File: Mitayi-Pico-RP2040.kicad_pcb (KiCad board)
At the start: 2 copper layers, 21 x 51 mm, 66 parts, among them J1 EXP8, J2 USB_C_Receptacle_USB2.0, J3 Header_1, J4 Header_2, J5 SWD, J6 USB_B_Micro, SW1 Reset, SW2 UBUT, U1 W25Q128JVS, U2 MIC5219-3.3YM5, U3 RP2040, Y1 YIC-12M20P2/XT324-10/10

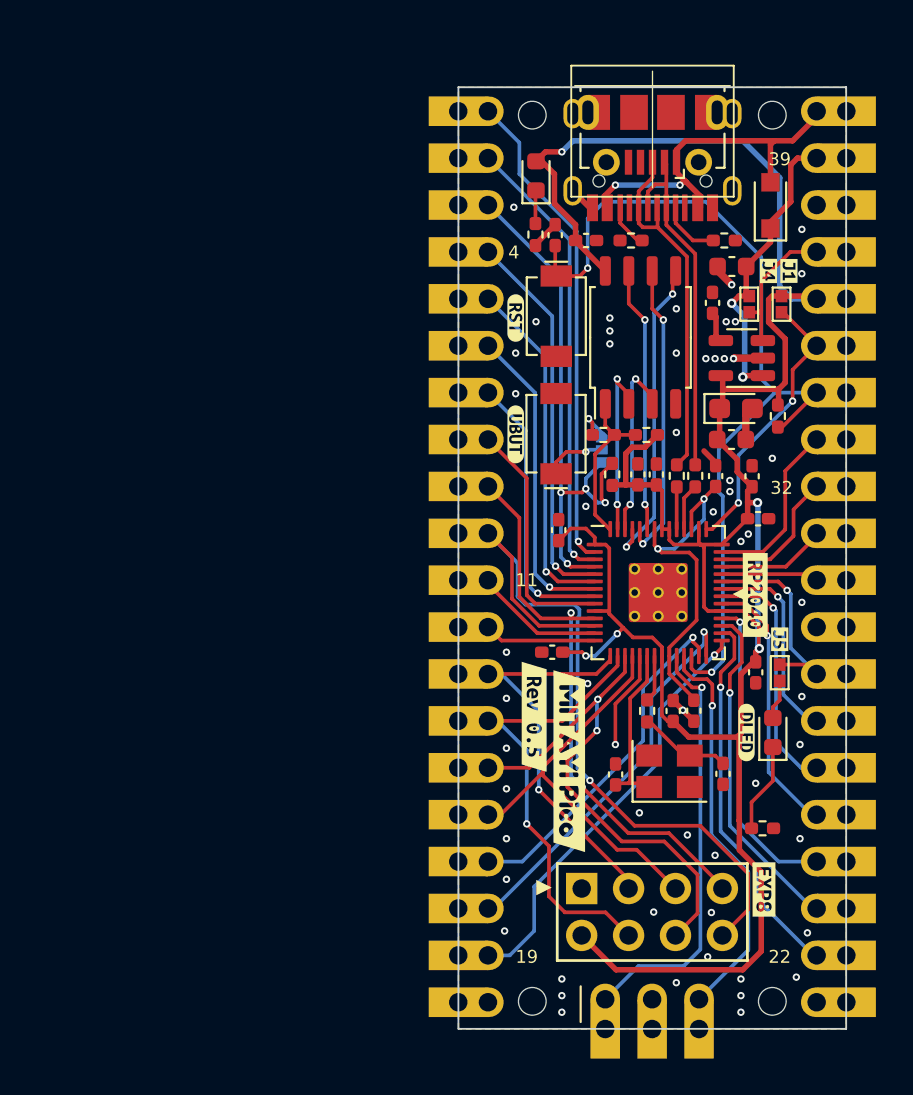
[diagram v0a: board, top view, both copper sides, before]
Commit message: Remove headers and much more
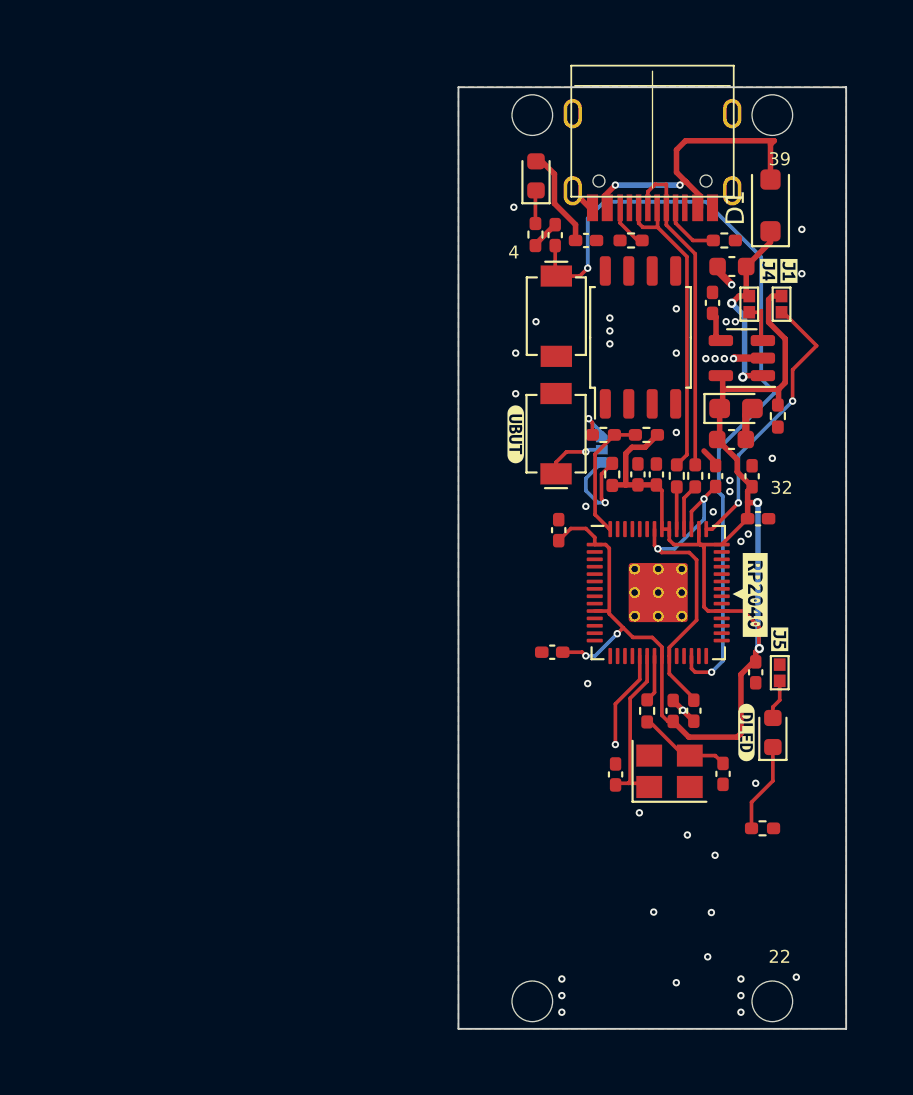
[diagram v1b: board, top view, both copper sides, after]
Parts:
- removed the G*** at (149.1, 89.7)
- removed J1: EXP8, Connector_PinHeader_2.54mm:PinHeader_2x04_P2.54mm_Vertical
- removed J3: Header_1, CIRCUITSTATE-Connector-Pin-Headers:PinHeader_1x20_2H_P2.54mm_Vertical
- removed J4: Header_2, CIRCUITSTATE-Connector-Pin-Headers:PinHeader_1x20_2H_P2.54mm_Vertical
- removed J5: SWD, Connector_PinHeader_2.54mm:PinHeader_1x03_P2.54mm_Vertical
- removed J6: USB_B_Micro, Connector_USB:USB_Micro-B_Molex-105017-0001
- removed kibuzzard-631DCCC7: G***, kibuzzard-631DCCC7
- removed kibuzzard-631DCE29: G***, kibuzzard-631DCE29
- removed kibuzzard-631DD065: G***, kibuzzard-631DD065
- removed kibuzzard-631DD76C: G***, kibuzzard-631DD76C
- removed kibuzzard-632C7F13: G***, kibuzzard-632C7F13
- removed kibuzzard-63B95AA9: G***, kibuzzard-63B95AA9
- D1: footprint Diode_SMD:D_SOD-323_HandSoldering -> Diode_SMD:D_SOD-123F
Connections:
- U1 pad 1: /QSPI_SS -> unconnected-(U1-~{CS}-Pad1)
- U1 pad 2: /QSPI_SD1 -> unconnected-(U1-DO(IO1)-Pad2)
- U1 pad 3: /QSPI_SD2 -> unconnected-(U1-IO2-Pad3)
- U1 pad 4: GND -> unconnected-(U1-GND-Pad4)
- U1 pad 5: /QSPI_SD0 -> unconnected-(U1-DI(IO0)-Pad5)
- U1 pad 6: /QSPI_SCLK -> unconnected-(U1-CLK-Pad6)
- U1 pad 7: /QSPI_SD3 -> unconnected-(U1-IO3-Pad7)
- U1 pad 8: +3V3 -> unconnected-(U1-VCC-Pad8)
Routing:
- net +3V3: track 135.6 -> 84.4 mm, vias 5 -> 4
- net /GPIO9: track 41.1 -> 0.00 mm, vias 1 -> 0
- net /GPIO8: track 31.2 -> 0.00 mm, vias 2 -> 0
- net /GPIO14: track 29.0 -> 0.00 mm, vias 2 -> 0
- net /GPIO0: track 26.5 -> 0.00 mm, vias 1 -> 0
- net /GPIO13: track 25.1 -> 0.00 mm, vias 1 -> 0
- net /GPIO1: track 24.6 -> 0.00 mm, vias 1 -> 0
- net /GPIO2: track 29.8 -> 5.65 mm, vias 4 -> 1
- net /SWCLK: track 23.1 -> 0.00 mm, vias 1 -> 0
- net /GPIO18: track 23.0 -> 0.00 mm, vias 1 -> 0
- net /GPIO12: track 22.4 -> 0.00 mm, vias 1 -> 0
- net /GPIO15: track 22.1 -> 0.00 mm
- net /SWDIO: track 21.6 -> 0.00 mm, vias 1 -> 0
- net /GPIO17: track 21.4 -> 0.00 mm, vias 1 -> 0
- net /GPIO3: track 20.8 -> 0.00 mm, vias 1 -> 0
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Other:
- board text removed: "11"
- board text removed: "19"
- board text removed: "3V3"
- board text removed: "AREF"
- board text removed: "Designed in KiCad"
- board text removed: "GND"
- board text removed: "GP0"
- board text removed: "GP1"
- board text removed: "GP10"
- board text removed: "GP11"
- board text removed: "GP12"
- board text removed: "GP13"
- board text removed: "GP14"
- board text removed: "GP15"
- board text removed: "GP16"
- board text removed: "GP17"
- board text removed: "GP18"
- board text removed: "GP19"
- board text removed: "GP2"
- board text removed: "GP20"
- board text removed: "GP21"
- board text removed: "GP22"
- board text removed: "GP23"
- board text removed: "GP24"
- board text removed: "GP25"
- board text removed: "GP26"
- board text removed: "GP27"
- board text removed: "GP28"
- board text removed: "GP29"
- board text removed: "GP3"
- board text removed: "GP4"
- board text removed: "GP5"
- board text removed: "GP6"
- board text removed: "GP7"
- board text removed: "GP8"
- board text removed: "GP9"
- board text removed: "RUN"
- board text removed: "VBUS"
- board text removed: "VSYS"
- board text removed: "V_EN"
- board text removed: "www.circuitstate.com"

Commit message: playing around with footprints
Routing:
- net +3V3: track 84.4 -> 98.3 mm, vias 4 -> 6
- net /GPIO2: track 5.65 -> 13.0 mm, vias 1 -> 2
- net /GPIO25: track 0.00 -> 6.05 mm
- net /RUN: track 43.4 -> 44.5 mm, vias 2 -> 3

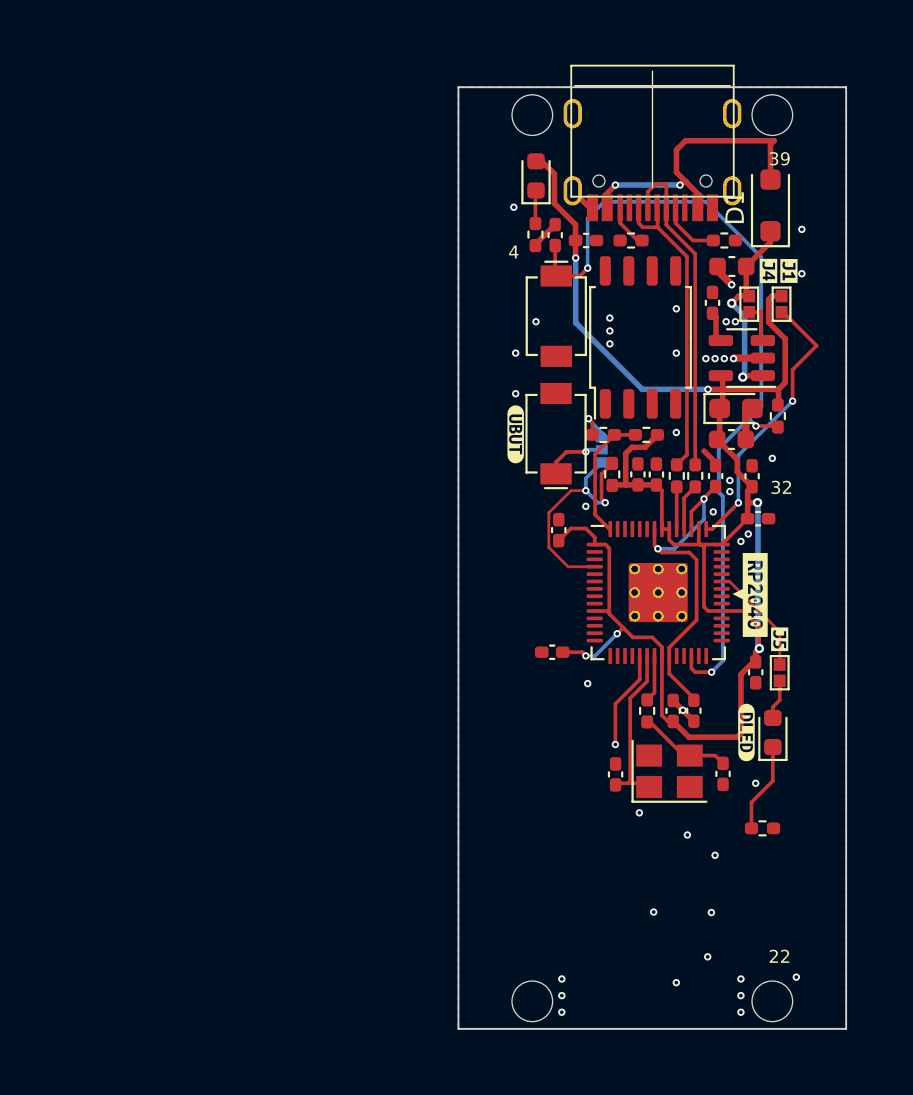
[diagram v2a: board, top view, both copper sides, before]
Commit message: Update footprints
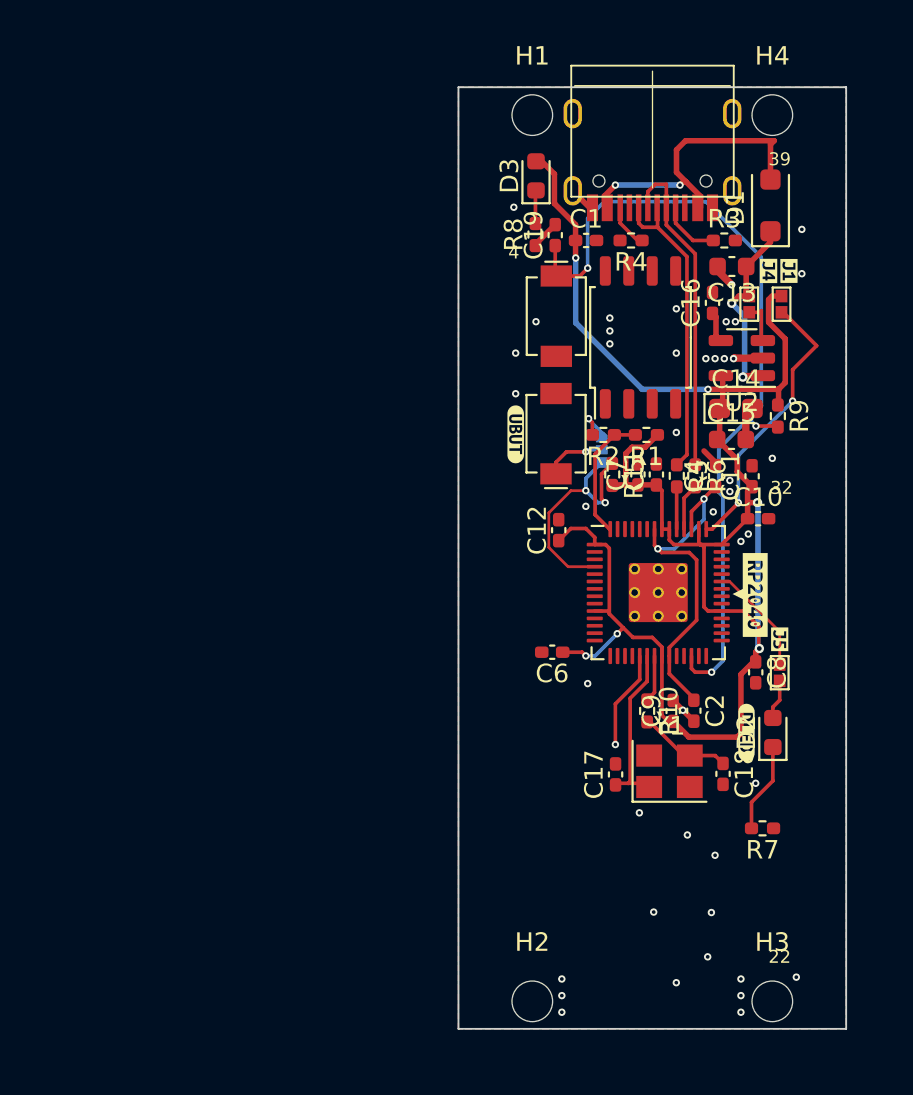
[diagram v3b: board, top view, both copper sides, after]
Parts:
- G***: footprint LOGO -> 00ProjectFootprints:LOGO
- J2: footprint CIRCUITSTATE_Connector_USB:Korean-Hroparts-Elec_TYPE-C-31-M-12 -> 00ProjectFootprints:Korean-Hroparts-Elec_TYPE-C-31-M-12
- U1: footprint Package_SO:SOIC-8_5.23x5.23mm_P1.27mm -> 00ProjectFootprints:SOIC-8_5.23x5.23mm_P1.27mm
- U3: footprint CIRCUITSTATE-QFN:RP2040-QFN-56 -> 00ProjectFootprints:RP2040-QFN-56
- kibuzzard-631DCCA6: footprint kibuzzard-631DCCA6 -> 00ProjectFootprints:kibuzzard-631DCCA6
- kibuzzard-631DCD0C: footprint kibuzzard-631DCD0C -> 00ProjectFootprints:kibuzzard-631DCD0C
- kibuzzard-631DCDA0: footprint kibuzzard-631DCDA0 -> 00ProjectFootprints:kibuzzard-631DCDA0
- kibuzzard-631DCDB3: footprint kibuzzard-631DCDB3 -> 00ProjectFootprints:kibuzzard-631DCDB3
- kibuzzard-631DCE60: footprint kibuzzard-631DCE60 -> 00ProjectFootprints:kibuzzard-631DCE60
- kibuzzard-632CA15B: footprint kibuzzard-632CA15B -> 00ProjectFootprints:kibuzzard-632CA15B

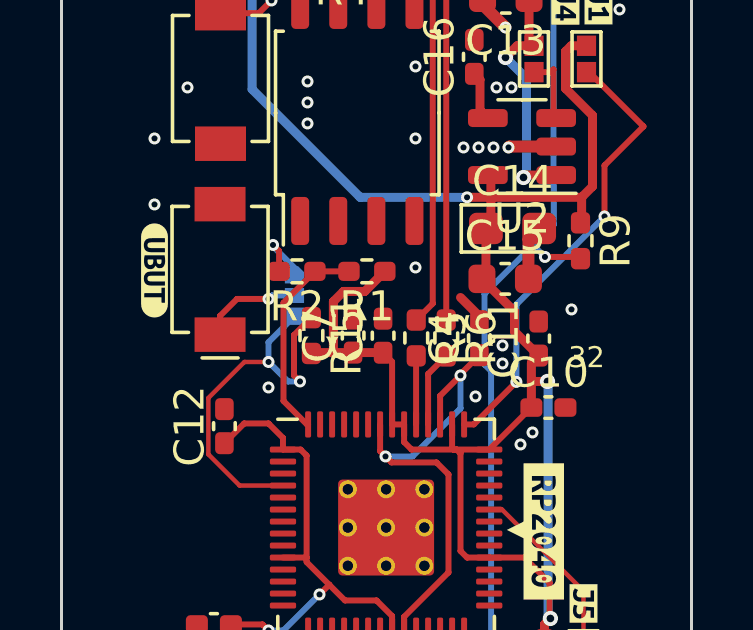
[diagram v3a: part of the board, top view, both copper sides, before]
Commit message: Simplyfix Boot Button
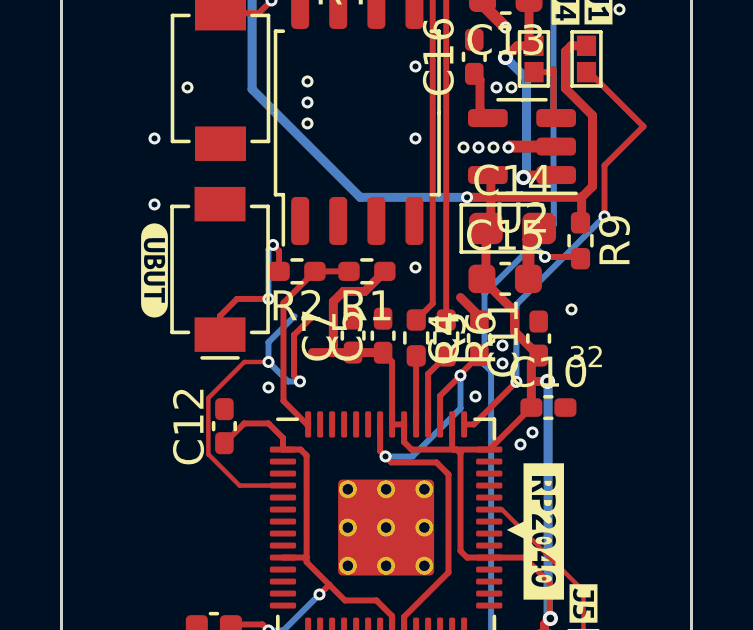
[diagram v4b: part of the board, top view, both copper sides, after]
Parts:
- removed JP6: UBUT_SEL, CIRCUITSTATE_Jumper_SMD:Solder-Jumper_3P_Open_0402
- removed R11: 5.1K, Resistor_SMD:R_0402_1005Metric_Pad0.72x0.64mm_HandSolder
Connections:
- SW2 pad 1: Net-(JP6-C) -> /~{USB_BOOT}
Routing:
- net Net-(JP6-C): track 3.39 -> 0.00 mm, vias 1 -> 0
- net /~{USB_BOOT}: track 2.26 -> 5.30 mm, vias 1 -> 2

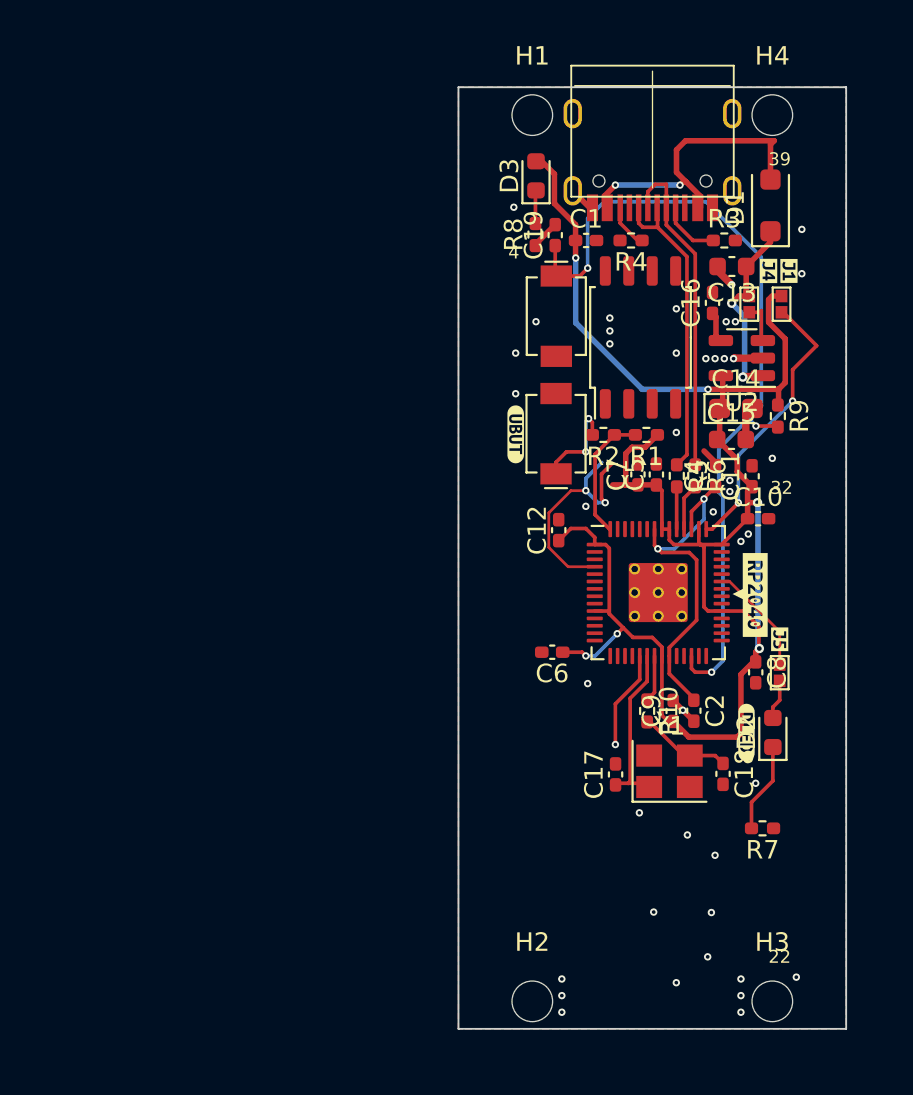
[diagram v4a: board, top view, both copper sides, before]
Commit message: Added more components
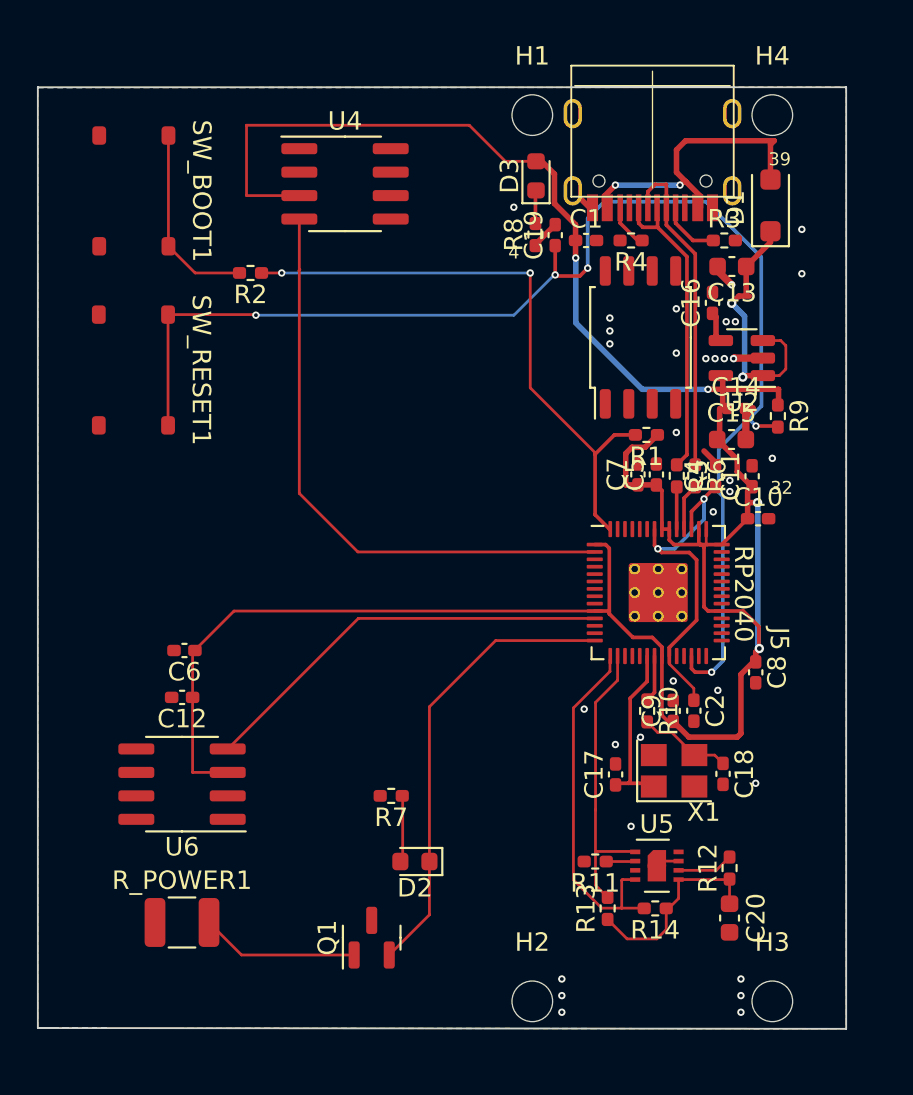
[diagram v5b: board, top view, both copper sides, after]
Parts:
- removed JP1: AREF_SEL, CIRCUITSTATE_Jumper_SMD:Solder-Jumper_2P_Open_0402
- removed JP4: VR1_CE, CIRCUITSTATE_Jumper_SMD:Solder-Jumper_2P_Open_0402
- removed JP5: DEB_EN, CIRCUITSTATE_Jumper_SMD:Solder-Jumper_2P_Open_0402
- removed SW1: Reset, CIRCUITSTATE_Switch_SMD:CK_SW_SPST_UK-B0273-SP25Y
- removed SW2: UBUT, CIRCUITSTATE_Switch_SMD:CK_SW_SPST_UK-B0273-SP25Y
- removed Y1: YIC-12M20P2/XT324-10/10, Crystal:Crystal_SMD_3225-4Pin_3.2x2.5mm
- removed kibuzzard-631DCCA6: G***, 00ProjectFootprints:kibuzzard-631DCCA6
- removed kibuzzard-631DCD0C: G***, 00ProjectFootprints:kibuzzard-631DCD0C
- removed kibuzzard-631DCDA0: G***, 00ProjectFootprints:kibuzzard-631DCDA0
- removed kibuzzard-631DCDB3: G***, 00ProjectFootprints:kibuzzard-631DCDB3
- removed kibuzzard-631DCE60: G***, 00ProjectFootprints:kibuzzard-631DCE60
- removed kibuzzard-632CA15B: G***, 00ProjectFootprints:kibuzzard-632CA15B
- added C20: 10u, Capacitor_SMD:C_0603_1608Metric, F.Cu at (151.4, 108.6)
- added Q1: NMOS, Package_TO_SOT_SMD:SOT-23, F.Cu at (132.0, 109.7)
- added R11: 10k, Resistor_SMD:R_0402_1005Metric_Pad0.72x0.64mm_HandSolder, F.Cu at (144.1, 105.5)
- added R12: 10k, Resistor_SMD:R_0402_1005Metric_Pad0.72x0.64mm_HandSolder, F.Cu at (151.4, 105.9)
- added R13: 10k, Resistor_SMD:R_0402_1005Metric_Pad0.72x0.64mm_HandSolder, F.Cu at (144.8, 108.1)
- added R14: 10k, Resistor_SMD:R_0402_1005Metric_Pad0.72x0.64mm_HandSolder, F.Cu at (147.4, 108.1)
- added R_POWER1: 125, Resistor_SMD:R_1210_3225Metric, F.Cu at (121.7, 108.8)
- added SW_BOOT1: Boot, 00_Project:TS-1187A-B-A-B, F.Cu at (128.0, 69.2)
- added SW_RESET1: Reset, 00_Project:TS-1187A-B-A-B, F.Cu at (128.0, 78.9)
- added U4: DS18B20Z, Package_SO:SOIC-8_3.9x4.9mm_P1.27mm, F.Cu at (130.6, 68.8)
- added U5: SHT31-DIS, Sensor_Humidity:Sensirion_DFN-8-1EP_2.5x2.5mm_P0.5mm_EP1.1x1.7mm, F.Cu at (147.4, 105.8)
- added U6: DS18B20Z, Package_SO:SOIC-8_3.9x4.9mm_P1.27mm, F.Cu at (121.7, 101.3)
- added X1: 12MHz Yangxing Tech X322512MSB4SI, Crystal:Crystal_SMD_3225-4Pin_3.2x2.5mm, F.Cu at (148.4, 100.6)
- C14: value 2.2uF -> 2.2u; footprint Capacitor_Tantalum_SMD:CP_EIA-2012-12_Kemet-R -> Capacitor_SMD:C_0402_1005Metric
- D2: value DBG_LED -> HEATING_LED
- moved C12 22.3 mm to (121.7, 96.6), turned to 180 degrees
- moved R2 21.0 mm to (125.4, 73.7)
- moved D2 20.6 mm to (134.3, 105.5), turned to 180 degrees
- moved R7 20.2 mm to (133.1, 102.0)
- moved C6 19.9 mm to (121.9, 94.1)
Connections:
- D2 pad 1: Net-(D2-K) -> /GPIO11
- R7 pad 1: GND -> Net-(D2-A)
- R7 pad 2: Net-(D2-K) -> GND
- U2 pad 3: /V_EN -> /VSYS
- U3 pad 43: /AREF -> +3V3
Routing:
- net +3V3: track 98.3 -> 139.6 mm, vias 6 -> 4
- net /GPIO0: track 0.00 -> 32.2 mm
- net /RUN: track 44.5 -> 72.4 mm, vias 3 -> 5
- net /QSPI_SS: track 7.03 -> 32.9 mm, vias 0 -> 2
- net /GPIO11: track 0.00 -> 24.8 mm
- net /GPIO8: track 0.00 -> 22.8 mm
- net /GPIO12: track 0.00 -> 19.4 mm
- net /GPIO13: track 0.00 -> 16.0 mm
- net /AREF: track 15.2 -> 0.00 mm, vias 2 -> 0
- net /GPIO2: track 13.0 -> 0.00 mm, vias 2 -> 0
- net +3.3V: track 0.00 -> 10.7 mm
- net Net-(Q1-D): track 0.00 -> 8.59 mm
- net /GPIO25: track 6.05 -> 0.00 mm
- net GND: track 15.4 -> 9.44 mm, vias 44 -> 33
- net /~{USB_BOOT}: track 5.30 -> 10.4 mm, vias 2 -> 0
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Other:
- board size 21 x 51 mm -> 43.8 x 51 mm
- board text added: "J5"
- board text added: "RP2040"
- board text removed: "22"
- board text removed: "▼"
